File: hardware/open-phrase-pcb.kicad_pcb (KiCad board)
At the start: 2 copper layers, 98 x 47 mm, 5 parts, among them J1 Conn_01x36, J2 Conn_01x36, J3 Conn_01x36, J4 Conn_01x36

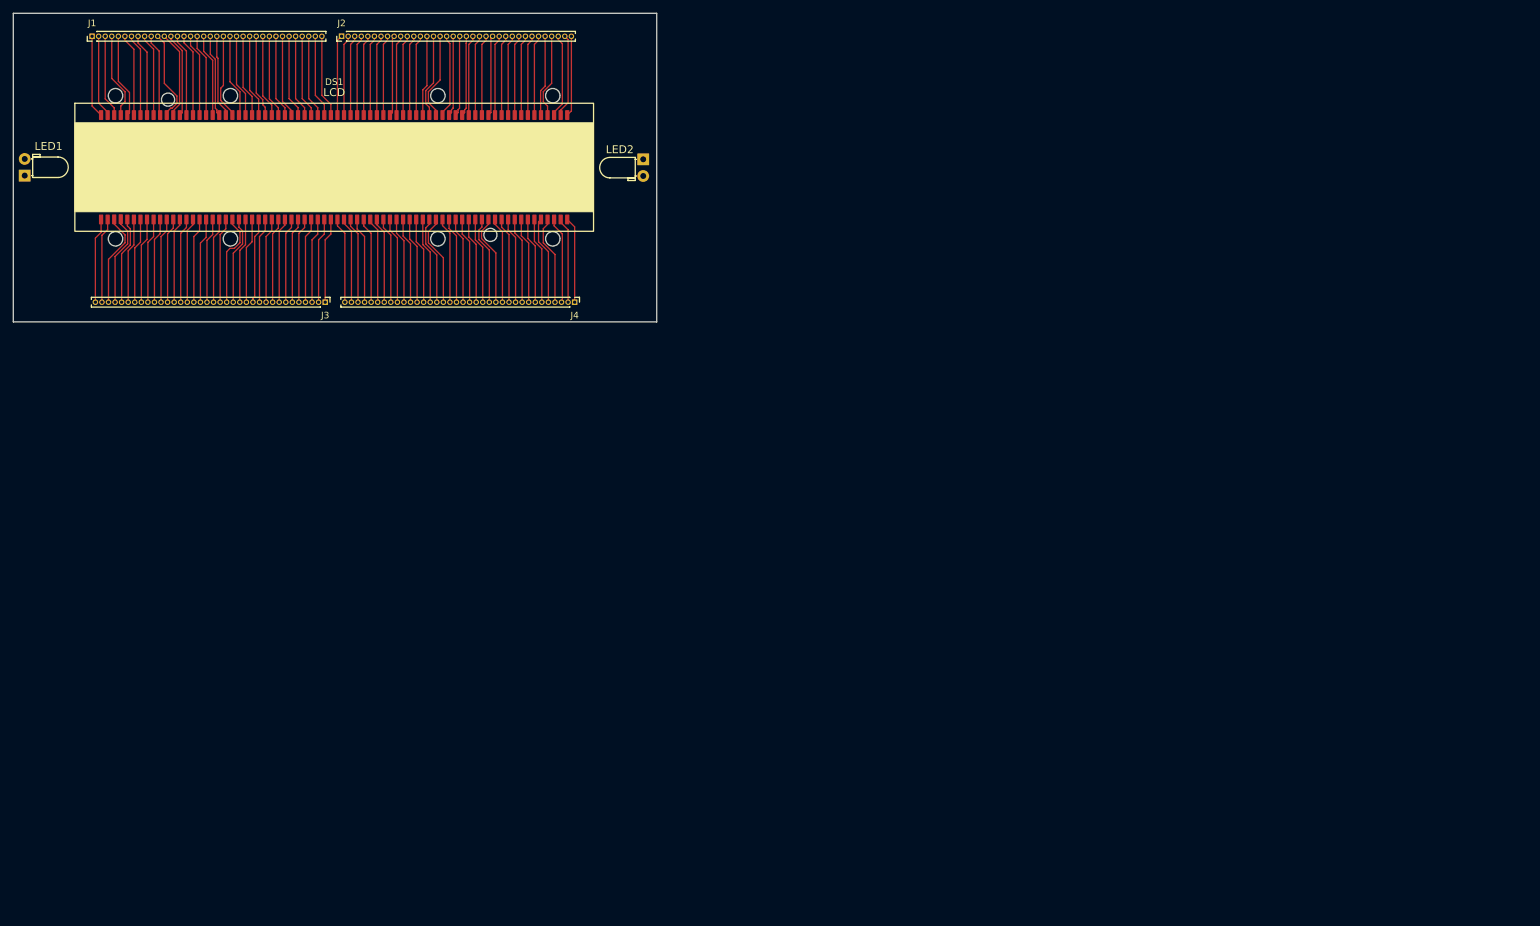
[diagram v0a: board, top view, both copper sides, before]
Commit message: 3d models and refining footprints
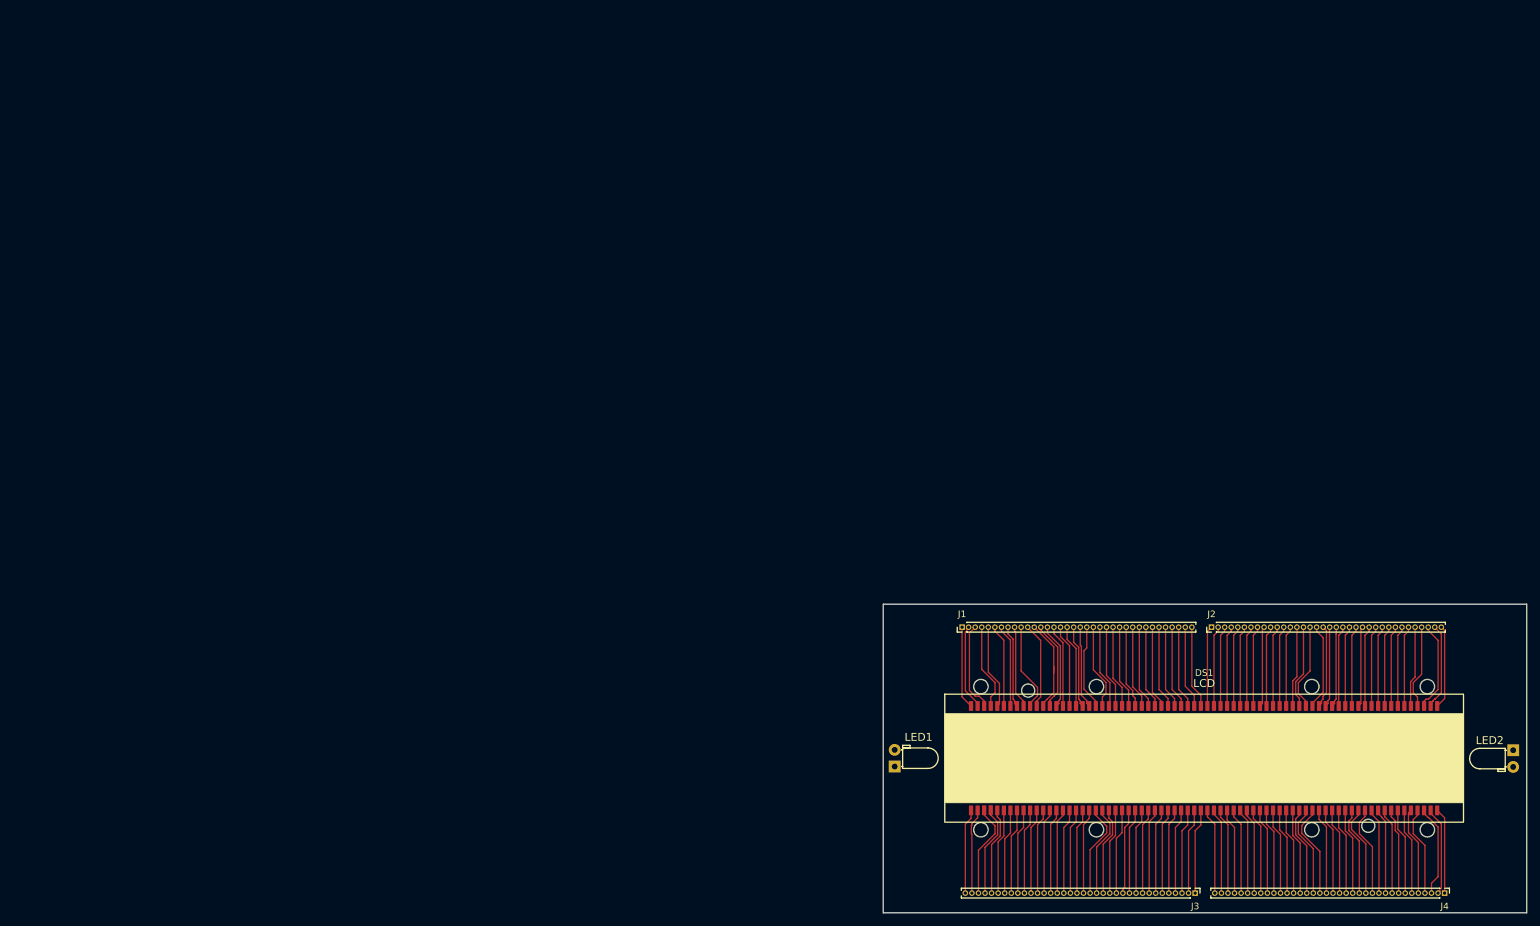
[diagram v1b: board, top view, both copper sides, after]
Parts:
- moved DS1 160.2 mm to (282.9, 164.9)
- moved J1 160.2 mm to (246.0, 145.0)
- moved J2 160.2 mm to (284.0, 145.0)
- moved J3 160.2 mm to (281.5, 185.5)
- moved J4 160.2 mm to (319.5, 185.5)
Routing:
- net Net-(J1-Pin_10): track 12.6 -> 14.3 mm
- net Net-(J3-Pin_17): track 13.0 -> 14.6 mm
- net Net-(J1-Pin_12): track 13.4 -> 14.9 mm
- net Net-(J4-Pin_3): track 13.2 -> 14.5 mm
- net Net-(J4-Pin_20): track 13.1 -> 14.4 mm
- net Net-(J1-Pin_3): track 12.6 -> 13.7 mm
- net Net-(J2-Pin_34): track 12.8 -> 13.7 mm
- net Net-(J1-Pin_11): track 14.0 -> 13.1 mm
- net Net-(J4-Pin_12): track 13.1 -> 13.8 mm
- net Net-(J1-Pin_13): track 12.9 -> 13.6 mm
- net Net-(J4-Pin_2): track 13.1 -> 13.6 mm
- net Net-(J1-Pin_2): track 12.6 -> 13.1 mm

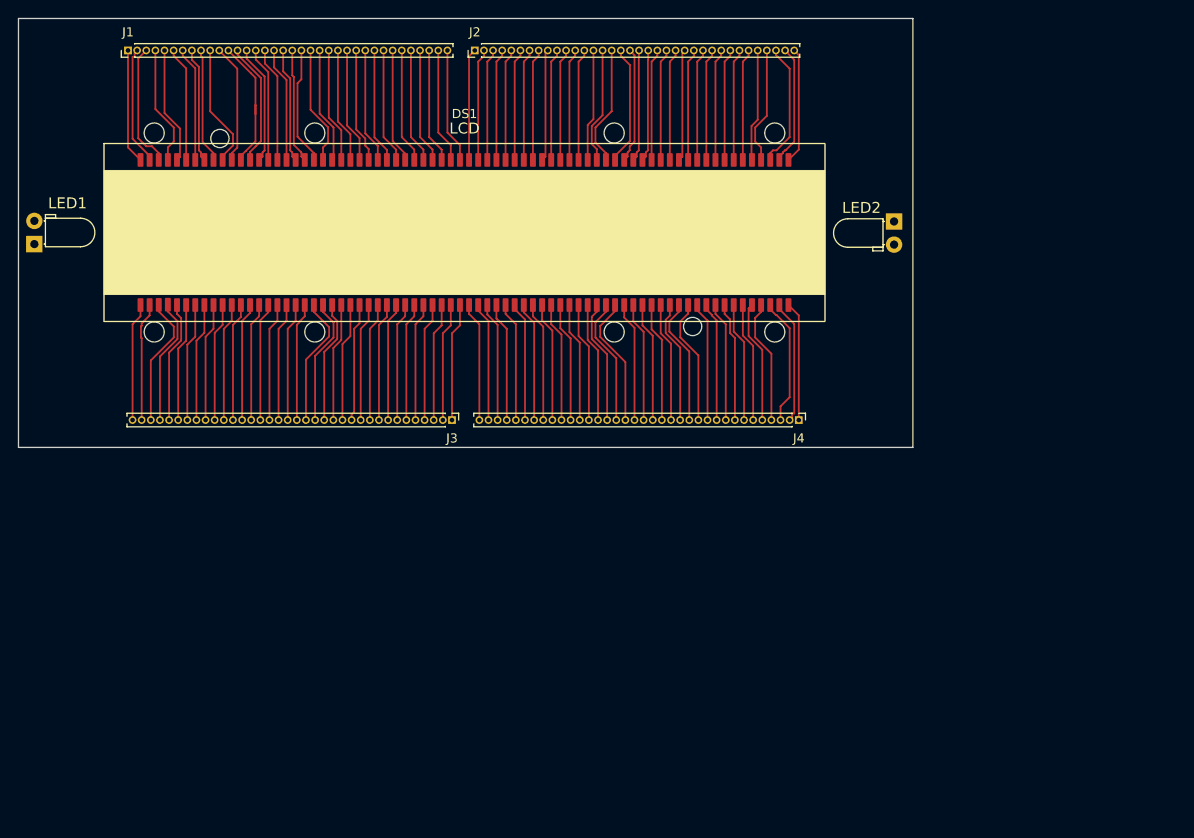
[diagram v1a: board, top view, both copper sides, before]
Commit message: Replicated PCB layout
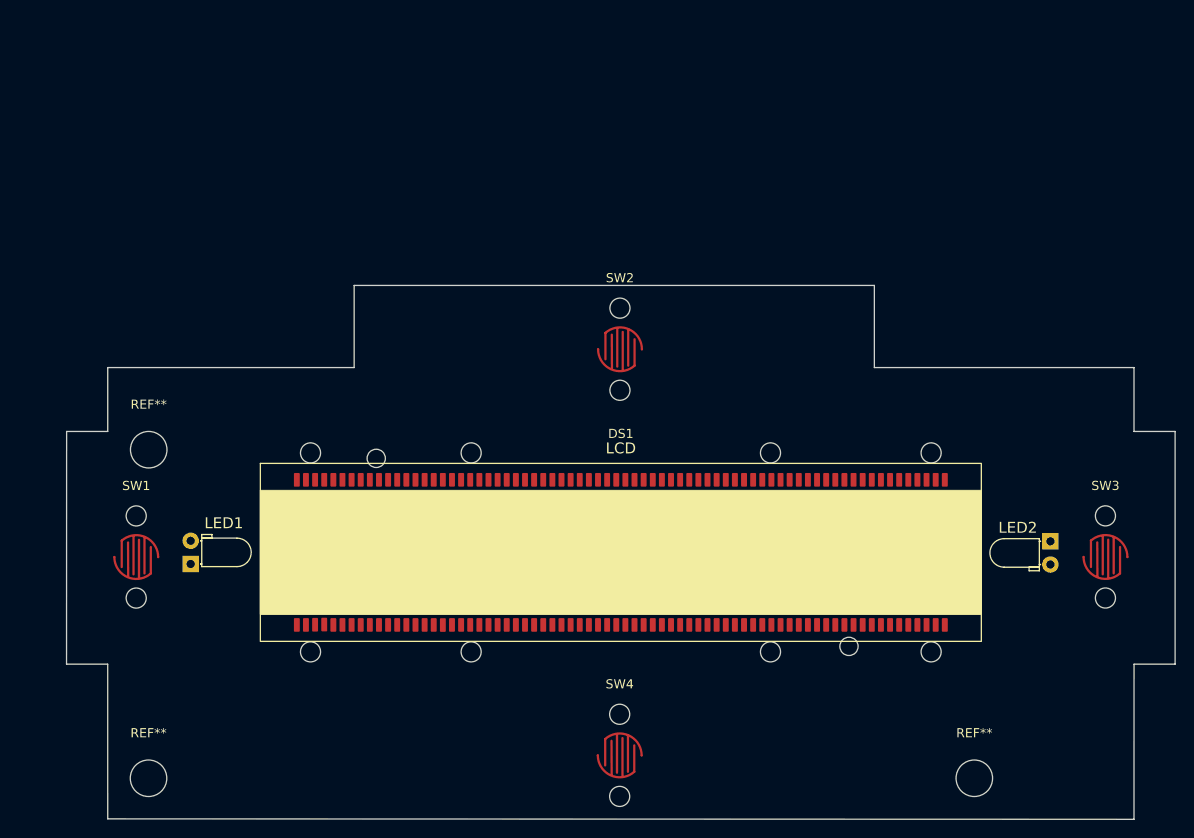
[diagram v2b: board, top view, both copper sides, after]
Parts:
- removed J1, J2, J3, J4: Conn_01x36, Connector_PinHeader_1.00mm:PinHeader_1x36_P1.00mm_Vertical
- added REF**: MountingHole_4mm, MountingHole:MountingHole_4mm, F.Cu at (248.3, 188.8)
- added REF**: MountingHole_4mm, MountingHole:MountingHole_4mm, F.Cu at (248.2, 224.8)
- added REF**: MountingHole_4mm, MountingHole:MountingHole_4mm, F.Cu at (338.7, 224.8)
- added SW1: SW_Push, custom-components:Switch_Pad_5x5mm_CaptiveMembrane_2x2mm_9mm, F.Cu at (246.9, 200.5)
- added SW2: SW_Push, custom-components:Switch_Pad_5x5mm_CaptiveMembrane_2x2mm_9mm, F.Cu at (299.9, 177.7)
- added SW3: SW_Push, custom-components:Switch_Pad_5x5mm_CaptiveMembrane_2x2mm_9mm, F.Cu at (353.1, 200.5)
- added SW4: SW_Push, custom-components:Switch_Pad_5x5mm_CaptiveMembrane_2x2mm_9mm, F.Cu at (299.9, 222.2)
- moved DS1 39.0 mm to (300.0, 200.0)
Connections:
- DS1 pad 1: Net-(J1-Pin_1) -> unconnected-(DS1-Pad1)
- DS1 pad 10: Net-(J3-Pin_32) -> unconnected-(DS1-Pad10)
- DS1 pad 100: Net-(J4-Pin_23) -> unconnected-(DS1-Pad100)
- DS1 pad 101: Net-(J2-Pin_15) -> unconnected-(DS1-Pad101)
- DS1 pad 102: Net-(J4-Pin_22) -> unconnected-(DS1-Pad102)
- DS1 pad 103: Net-(J2-Pin_16) -> unconnected-(DS1-Pad103)
- DS1 pad 104: Net-(J4-Pin_21) -> unconnected-(DS1-Pad104)
- DS1 pad 105: Net-(J2-Pin_17) -> unconnected-(DS1-Pad105)
- DS1 pad 106: Net-(J4-Pin_20) -> unconnected-(DS1-Pad106)
- DS1 pad 107: Net-(J2-Pin_18) -> unconnected-(DS1-Pad107)
- DS1 pad 108: Net-(J4-Pin_19) -> unconnected-(DS1-Pad108)
- DS1 pad 109: Net-(J2-Pin_19) -> unconnected-(DS1-Pad109)
- DS1 pad 11: Net-(J1-Pin_6) -> unconnected-(DS1-Pad11)
- DS1 pad 110: Net-(J4-Pin_18) -> unconnected-(DS1-Pad110)
- DS1 pad 111: Net-(J2-Pin_20) -> unconnected-(DS1-Pad111)
- DS1 pad 112: Net-(J4-Pin_17) -> unconnected-(DS1-Pad112)
- DS1 pad 113: Net-(J2-Pin_21) -> unconnected-(DS1-Pad113)
- DS1 pad 114: Net-(J4-Pin_16) -> unconnected-(DS1-Pad114)
- DS1 pad 115: Net-(J2-Pin_22) -> unconnected-(DS1-Pad115)
- DS1 pad 116: Net-(J4-Pin_15) -> unconnected-(DS1-Pad116)
- DS1 pad 117: Net-(J2-Pin_23) -> unconnected-(DS1-Pad117)
- DS1 pad 118: Net-(J4-Pin_14) -> unconnected-(DS1-Pad118)
- DS1 pad 119: Net-(J2-Pin_24) -> unconnected-(DS1-Pad119)
- DS1 pad 12: Net-(J3-Pin_31) -> unconnected-(DS1-Pad12)
- DS1 pad 120: Net-(J4-Pin_13) -> unconnected-(DS1-Pad120)
- DS1 pad 121: Net-(J2-Pin_25) -> unconnected-(DS1-Pad121)
- DS1 pad 122: Net-(J4-Pin_12) -> unconnected-(DS1-Pad122)
- DS1 pad 123: Net-(J2-Pin_26) -> unconnected-(DS1-Pad123)
- DS1 pad 124: Net-(J4-Pin_11) -> unconnected-(DS1-Pad124)
- DS1 pad 125: Net-(J2-Pin_27) -> unconnected-(DS1-Pad125)
- DS1 pad 126: Net-(J4-Pin_10) -> unconnected-(DS1-Pad126)
- DS1 pad 127: Net-(J2-Pin_28) -> unconnected-(DS1-Pad127)
- DS1 pad 128: Net-(J4-Pin_9) -> unconnected-(DS1-Pad128)
- DS1 pad 129: Net-(J2-Pin_29) -> unconnected-(DS1-Pad129)
- DS1 pad 13: Net-(J1-Pin_7) -> unconnected-(DS1-Pad13)
- DS1 pad 130: Net-(J4-Pin_8) -> unconnected-(DS1-Pad130)
- DS1 pad 131: Net-(J2-Pin_30) -> unconnected-(DS1-Pad131)
- DS1 pad 132: Net-(J4-Pin_7) -> unconnected-(DS1-Pad132)
- DS1 pad 133: Net-(J2-Pin_31) -> unconnected-(DS1-Pad133)
- DS1 pad 134: Net-(J4-Pin_6) -> unconnected-(DS1-Pad134)
- DS1 pad 135: Net-(J2-Pin_32) -> unconnected-(DS1-Pad135)
- DS1 pad 136: Net-(J4-Pin_5) -> unconnected-(DS1-Pad136)
- DS1 pad 137: Net-(J2-Pin_33) -> unconnected-(DS1-Pad137)
- DS1 pad 138: Net-(J4-Pin_4) -> unconnected-(DS1-Pad138)
- DS1 pad 139: Net-(J2-Pin_34) -> unconnected-(DS1-Pad139)
- DS1 pad 14: Net-(J3-Pin_30) -> unconnected-(DS1-Pad14)
- DS1 pad 140: Net-(J4-Pin_3) -> unconnected-(DS1-Pad140)
- DS1 pad 141: Net-(J2-Pin_35) -> unconnected-(DS1-Pad141)
- DS1 pad 142: Net-(J4-Pin_2) -> unconnected-(DS1-Pad142)
- DS1 pad 143: Net-(J2-Pin_36) -> unconnected-(DS1-Pad143)
- DS1 pad 144: Net-(J4-Pin_1) -> unconnected-(DS1-Pad144)
- DS1 pad 15: Net-(J1-Pin_8) -> unconnected-(DS1-Pad15)
- DS1 pad 16: Net-(J3-Pin_29) -> unconnected-(DS1-Pad16)
- DS1 pad 17: Net-(J1-Pin_9) -> unconnected-(DS1-Pad17)
- DS1 pad 18: Net-(J3-Pin_28) -> unconnected-(DS1-Pad18)
- DS1 pad 19: Net-(J1-Pin_10) -> unconnected-(DS1-Pad19)
- DS1 pad 2: Net-(J3-Pin_36) -> unconnected-(DS1-Pad2)
- DS1 pad 20: Net-(J3-Pin_27) -> unconnected-(DS1-Pad20)
- DS1 pad 21: Net-(J1-Pin_11) -> unconnected-(DS1-Pad21)
- DS1 pad 22: Net-(J3-Pin_26) -> unconnected-(DS1-Pad22)
- DS1 pad 23: Net-(J1-Pin_12) -> unconnected-(DS1-Pad23)
- DS1 pad 24: Net-(J3-Pin_25) -> unconnected-(DS1-Pad24)
- DS1 pad 25: Net-(J1-Pin_13) -> unconnected-(DS1-Pad25)
- DS1 pad 26: Net-(J3-Pin_24) -> unconnected-(DS1-Pad26)
- DS1 pad 27: Net-(J1-Pin_14) -> unconnected-(DS1-Pad27)
- DS1 pad 28: Net-(J3-Pin_23) -> unconnected-(DS1-Pad28)
- DS1 pad 29: Net-(J1-Pin_15) -> unconnected-(DS1-Pad29)
- DS1 pad 3: Net-(J1-Pin_2) -> unconnected-(DS1-Pad3)
- DS1 pad 30: Net-(J3-Pin_22) -> unconnected-(DS1-Pad30)
- DS1 pad 31: Net-(J1-Pin_16) -> unconnected-(DS1-Pad31)
- DS1 pad 32: Net-(J3-Pin_21) -> unconnected-(DS1-Pad32)
- DS1 pad 33: Net-(J1-Pin_17) -> unconnected-(DS1-Pad33)
- DS1 pad 34: Net-(J3-Pin_20) -> unconnected-(DS1-Pad34)
- DS1 pad 35: Net-(J1-Pin_18) -> unconnected-(DS1-Pad35)
- DS1 pad 36: Net-(J3-Pin_19) -> unconnected-(DS1-Pad36)
- DS1 pad 37: Net-(J1-Pin_19) -> unconnected-(DS1-Pad37)
- DS1 pad 38: Net-(J3-Pin_18) -> unconnected-(DS1-Pad38)
- DS1 pad 39: Net-(J1-Pin_20) -> unconnected-(DS1-Pad39)
- DS1 pad 4: Net-(J3-Pin_35) -> unconnected-(DS1-Pad4)
- DS1 pad 40: Net-(J3-Pin_17) -> unconnected-(DS1-Pad40)
- DS1 pad 41: Net-(J1-Pin_21) -> unconnected-(DS1-Pad41)
- DS1 pad 42: Net-(J3-Pin_16) -> unconnected-(DS1-Pad42)
- DS1 pad 43: Net-(J1-Pin_22) -> unconnected-(DS1-Pad43)
- DS1 pad 44: Net-(J3-Pin_15) -> unconnected-(DS1-Pad44)
- DS1 pad 45: Net-(J1-Pin_23) -> unconnected-(DS1-Pad45)
- DS1 pad 46: Net-(J3-Pin_14) -> unconnected-(DS1-Pad46)
- DS1 pad 47: Net-(J1-Pin_24) -> unconnected-(DS1-Pad47)
- DS1 pad 48: Net-(J3-Pin_13) -> unconnected-(DS1-Pad48)
- DS1 pad 49: Net-(J1-Pin_25) -> unconnected-(DS1-Pad49)
- DS1 pad 5: Net-(J1-Pin_3) -> unconnected-(DS1-Pad5)
- DS1 pad 50: Net-(J3-Pin_12) -> unconnected-(DS1-Pad50)
- DS1 pad 51: Net-(J1-Pin_26) -> unconnected-(DS1-Pad51)
- DS1 pad 52: Net-(J3-Pin_11) -> unconnected-(DS1-Pad52)
- DS1 pad 53: Net-(J1-Pin_27) -> unconnected-(DS1-Pad53)
- DS1 pad 54: Net-(J3-Pin_10) -> unconnected-(DS1-Pad54)
- DS1 pad 55: Net-(J1-Pin_28) -> unconnected-(DS1-Pad55)
- DS1 pad 56: Net-(J3-Pin_9) -> unconnected-(DS1-Pad56)
- DS1 pad 57: Net-(J1-Pin_29) -> unconnected-(DS1-Pad57)
- DS1 pad 58: Net-(J3-Pin_8) -> unconnected-(DS1-Pad58)
- DS1 pad 59: Net-(J1-Pin_30) -> unconnected-(DS1-Pad59)
- DS1 pad 6: Net-(J3-Pin_34) -> unconnected-(DS1-Pad6)
- DS1 pad 60: Net-(J3-Pin_7) -> unconnected-(DS1-Pad60)
- DS1 pad 61: Net-(J1-Pin_31) -> unconnected-(DS1-Pad61)
- DS1 pad 62: Net-(J3-Pin_6) -> unconnected-(DS1-Pad62)
- DS1 pad 63: Net-(J1-Pin_32) -> unconnected-(DS1-Pad63)
- DS1 pad 64: Net-(J3-Pin_5) -> unconnected-(DS1-Pad64)
- DS1 pad 65: Net-(J1-Pin_33) -> unconnected-(DS1-Pad65)
- DS1 pad 66: Net-(J3-Pin_4) -> unconnected-(DS1-Pad66)
- DS1 pad 67: Net-(J1-Pin_34) -> unconnected-(DS1-Pad67)
- DS1 pad 68: Net-(J3-Pin_3) -> unconnected-(DS1-Pad68)
- DS1 pad 69: Net-(J1-Pin_35) -> unconnected-(DS1-Pad69)
- DS1 pad 7: Net-(J1-Pin_4) -> unconnected-(DS1-Pad7)
- DS1 pad 70: Net-(J3-Pin_2) -> unconnected-(DS1-Pad70)
- DS1 pad 71: Net-(J1-Pin_36) -> unconnected-(DS1-Pad71)
- DS1 pad 72: Net-(J3-Pin_1) -> unconnected-(DS1-Pad72)
- DS1 pad 73: Net-(J2-Pin_1) -> unconnected-(DS1-Pad73)
- DS1 pad 74: Net-(J4-Pin_36) -> unconnected-(DS1-Pad74)
- DS1 pad 75: Net-(J2-Pin_2) -> unconnected-(DS1-Pad75)
- DS1 pad 76: Net-(J4-Pin_35) -> unconnected-(DS1-Pad76)
- DS1 pad 77: Net-(J2-Pin_3) -> unconnected-(DS1-Pad77)
- DS1 pad 78: Net-(J4-Pin_34) -> unconnected-(DS1-Pad78)
- DS1 pad 79: Net-(J2-Pin_4) -> unconnected-(DS1-Pad79)
- DS1 pad 8: Net-(J3-Pin_33) -> unconnected-(DS1-Pad8)
- DS1 pad 80: Net-(J4-Pin_33) -> unconnected-(DS1-Pad80)
- DS1 pad 81: Net-(J2-Pin_5) -> unconnected-(DS1-Pad81)
- DS1 pad 82: Net-(J4-Pin_32) -> unconnected-(DS1-Pad82)
- DS1 pad 83: Net-(J2-Pin_6) -> unconnected-(DS1-Pad83)
- DS1 pad 84: Net-(J4-Pin_31) -> unconnected-(DS1-Pad84)
- DS1 pad 85: Net-(J2-Pin_7) -> unconnected-(DS1-Pad85)
- DS1 pad 86: Net-(J4-Pin_30) -> unconnected-(DS1-Pad86)
- DS1 pad 87: Net-(J2-Pin_8) -> unconnected-(DS1-Pad87)
- DS1 pad 88: Net-(J4-Pin_29) -> unconnected-(DS1-Pad88)
- DS1 pad 89: Net-(J2-Pin_9) -> unconnected-(DS1-Pad89)
- DS1 pad 9: Net-(J1-Pin_5) -> unconnected-(DS1-Pad9)
- DS1 pad 90: Net-(J4-Pin_28) -> unconnected-(DS1-Pad90)
- DS1 pad 91: Net-(J2-Pin_10) -> unconnected-(DS1-Pad91)
- DS1 pad 92: Net-(J4-Pin_27) -> unconnected-(DS1-Pad92)
- DS1 pad 93: Net-(J2-Pin_11) -> unconnected-(DS1-Pad93)
- DS1 pad 94: Net-(J4-Pin_26) -> unconnected-(DS1-Pad94)
- DS1 pad 95: Net-(J2-Pin_12) -> unconnected-(DS1-Pad95)
- DS1 pad 96: Net-(J4-Pin_25) -> unconnected-(DS1-Pad96)
- DS1 pad 97: Net-(J2-Pin_13) -> unconnected-(DS1-Pad97)
- DS1 pad 98: Net-(J4-Pin_24) -> unconnected-(DS1-Pad98)
- DS1 pad 99: Net-(J2-Pin_14) -> unconnected-(DS1-Pad99)
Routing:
- net Net-(J1-Pin_12): track 14.9 -> 0.00 mm
- net Net-(J3-Pin_17): track 14.6 -> 0.00 mm
- net Net-(J4-Pin_3): track 14.5 -> 0.00 mm
- net Net-(J4-Pin_20): track 14.4 -> 0.00 mm
- net Net-(J3-Pin_34): track 14.3 -> 0.00 mm
- net Net-(J1-Pin_10): track 14.3 -> 0.00 mm
- net Net-(J4-Pin_21): track 14.0 -> 0.00 mm
- net Net-(J4-Pin_13): track 13.9 -> 0.00 mm
- net Net-(J3-Pin_16): track 13.9 -> 0.00 mm
- net Net-(J3-Pin_33): track 13.9 -> 0.00 mm
- net Net-(J4-Pin_12): track 13.8 -> 0.00 mm
- net Net-(J2-Pin_34): track 13.7 -> 0.00 mm
- net Net-(J1-Pin_3): track 13.7 -> 0.00 mm
- net Net-(J4-Pin_2): track 13.6 -> 0.00 mm
- net Net-(J4-Pin_4): track 13.6 -> 0.00 mm
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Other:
- board size 98 x 47 mm -> 121.5 x 58.5 mm
